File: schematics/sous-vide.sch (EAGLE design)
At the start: 32 parts, among them IC1 MEGA8-P, T1 BC547, T2 BC547, T3 BC547

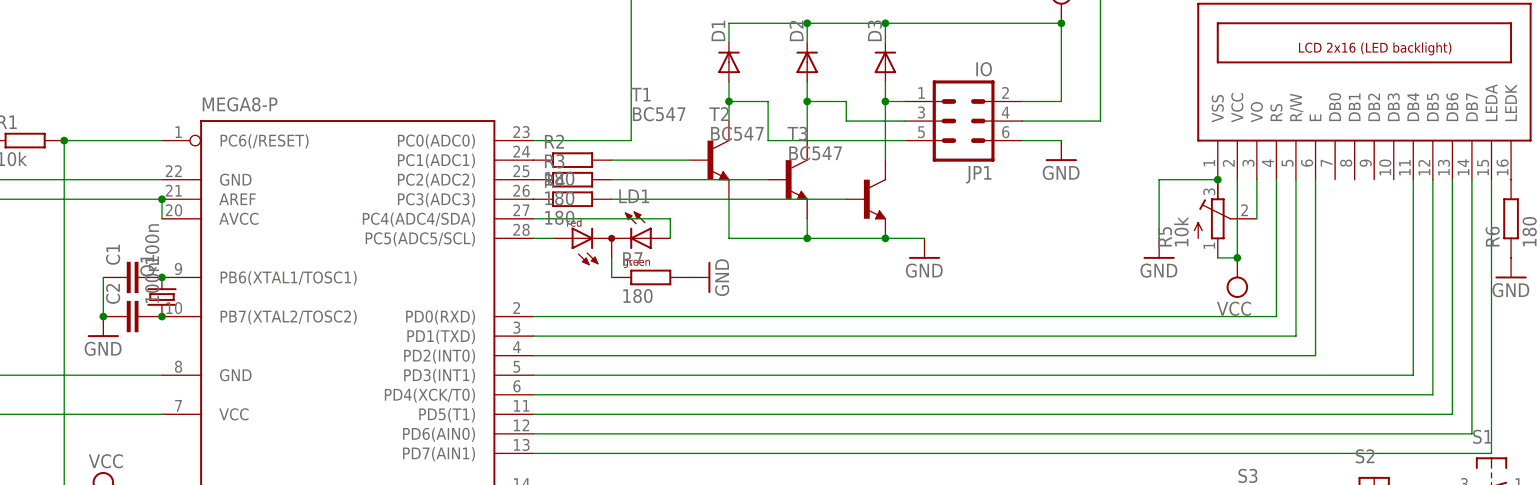
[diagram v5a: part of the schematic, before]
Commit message: Optimized traces and button definitions and send to pcb production as version 1.5
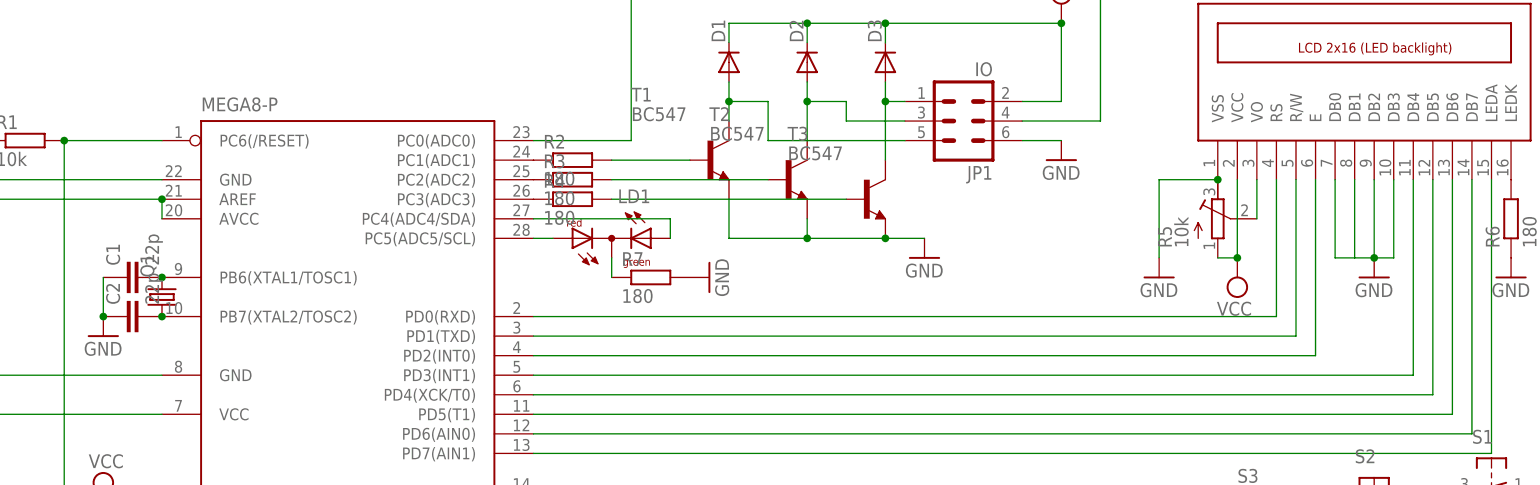
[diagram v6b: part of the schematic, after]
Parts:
- C1, C2: value 100n -> 22p
- R1, R6, R7: device rcl:R-EU_0207/2V -> rcl:R-EU_0207/7
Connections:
- net GND: now also LCD1.DB0, LCD1.DB1, LCD1.DB2, LCD1.DB3
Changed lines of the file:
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@@
 <parts>
 <part name="SUPPLY2" library="supply2" deviceset="VCC" device=""/>
-<part name="R1" library="rcl" deviceset="R-EU_" device="0207/2V" value="10k"/>
+<part name="R1" library="rcl" deviceset="R-EU_" device="0207/7" value="10k"/>
 <part name="GND7" library="supply1" deviceset="GND" device=""/>
-<part name="R7" library="rcl" deviceset="R-EU_" device="0207/2V" value="180"/>
+<part name="R7" library="rcl" deviceset="R-EU_" device="0207/7" value="180"/>
 <part name="GND3" library="supply1" deviceset="GND" device=""/>
 <part name="R5" library="resistor" deviceset="R-TRIMM" device="3339P" value="10k"/>
-<part name="R6" library="rcl" deviceset="R-EU_" device="0207/2V" value="180"/>
+<part name="R6" library="rcl" deviceset="R-EU_" device="0207/7" value="180"/>
 <part name="SUPPLY3" library="supply2" deviceset="VCC" device=""/>
 <part name="GND5" library="supply1" deviceset="GND" device=""/>
@@
 <part name="C3" library="resistor" deviceset="C-EU" device="025-025X050" value="100n"/>
 <part name="Q1" library="crystal" deviceset="CRYSTAL" device="HC49U-V"/>
-<part name="C1" library="resistor" deviceset="C-EU" device="025-025X050" value="100n"/>
-<part name="C2" library="resistor" deviceset="C-EU" device="025-025X050" value="100n"/>
+<part name="C1" library="resistor" deviceset="C-EU" device="025-025X050" value="22p"/>
+<part name="C2" library="resistor" deviceset="C-EU" device="025-025X050" value="22p"/>
 <part name="GND6" library="supply1" deviceset="GND" device=""/>
+<part name="GND11" library="supply1" deviceset="GND" device=""/>
 </parts>
 <sheets>
@@
 <instance part="GND7" gate="1" x="0" y="33.02"/>
 <instance part="R7" gate="G$1" x="86.36" y="73.66"/>
-<instance part="GND3" gate="1" x="152.4" y="76.2"/>
+<instance part="GND3" gate="1" x="152.4" y="73.66"/>
 <instance part="R5" gate="G$1" x="160.02" y="81.28"/>
 <instance part="R6" gate="G$1" x="198.12" y="81.28" rot="R90"/>
@@
 <instance part="C2" gate="G$1" x="17.78" y="68.58" rot="R90"/>
 <instance part="GND6" gate="1" x="15.24" y="66.04"/>
+<instance part="GND11" gate="1" x="180.34" y="73.66"/>
 </instances>
 <busses>
@@
 <segment>
 <pinref part="GND3" gate="1" pin="GND"/>
-<wire x1="152.4" y1="78.74" x2="152.4" y2="86.36" width="0.1524" layer="91"/>
+<wire x1="152.4" y1="76.2" x2="152.4" y2="86.36" width="0.1524" layer="91"/>
 <pinref part="R5" gate="G$1" pin="A"/>
 <wire x1="152.4" y1="86.36" x2="160.02" y2="86.36" width="0.1524" layer="91"/>
@@
 <junction x="15.24" y="68.58"/>
 </segment>
+<segment>
+<pinref part="LCD1" gate="G$1" pin="DB2"/>
+<pinref part="GND11" gate="1" pin="GND"/>
+<wire x1="180.34" y1="76.2" x2="180.34" y2="86.36" width="0.1524" layer="91"/>
+<pinref part="LCD1" gate="G$1" pin="DB3"/>
+<wire x1="182.88" y1="86.36" x2="182.88" y2="76.2" width="0.1524" layer="91"/>
+<wire x1="182.88" y1="76.2" x2="180.34" y2="76.2" width="0.1524" layer="91"/>
+<pinref part="LCD1" gate="G$1" pin="DB1"/>
+<wire x1="177.8" y1="86.36" x2="177.8" y2="76.2" width="0.1524" layer="91"/>
+<wire x1="177.8" y1="76.2" x2="180.34" y2="76.2" width="0.1524" layer="91"/>
+<pinref part="LCD1" gate="G$1" pin="DB0"/>
+<wire x1="175.26" y1="86.36" x2="175.26" y2="76.2" width="0.1524" layer="91"/>
+<wire x1="175.26" y1="76.2" x2="177.8" y2="76.2" width="0.1524" layer="91"/>
+<junction x="180.34" y="76.2"/>
+</segment>
 </net>
